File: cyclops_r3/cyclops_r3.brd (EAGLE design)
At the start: 124.5 x 79.9 mm, 113 parts, among them Q1 BC817, Q2 IRF510, U1 MCP4921, U10 ADG3301, U2 MCP4022-50k, U3 317-N, U4 TLV3701, U5 337-N, U6 ADR03, U7 OP1177, U8 LTC2052HV, U9 ZXTD45

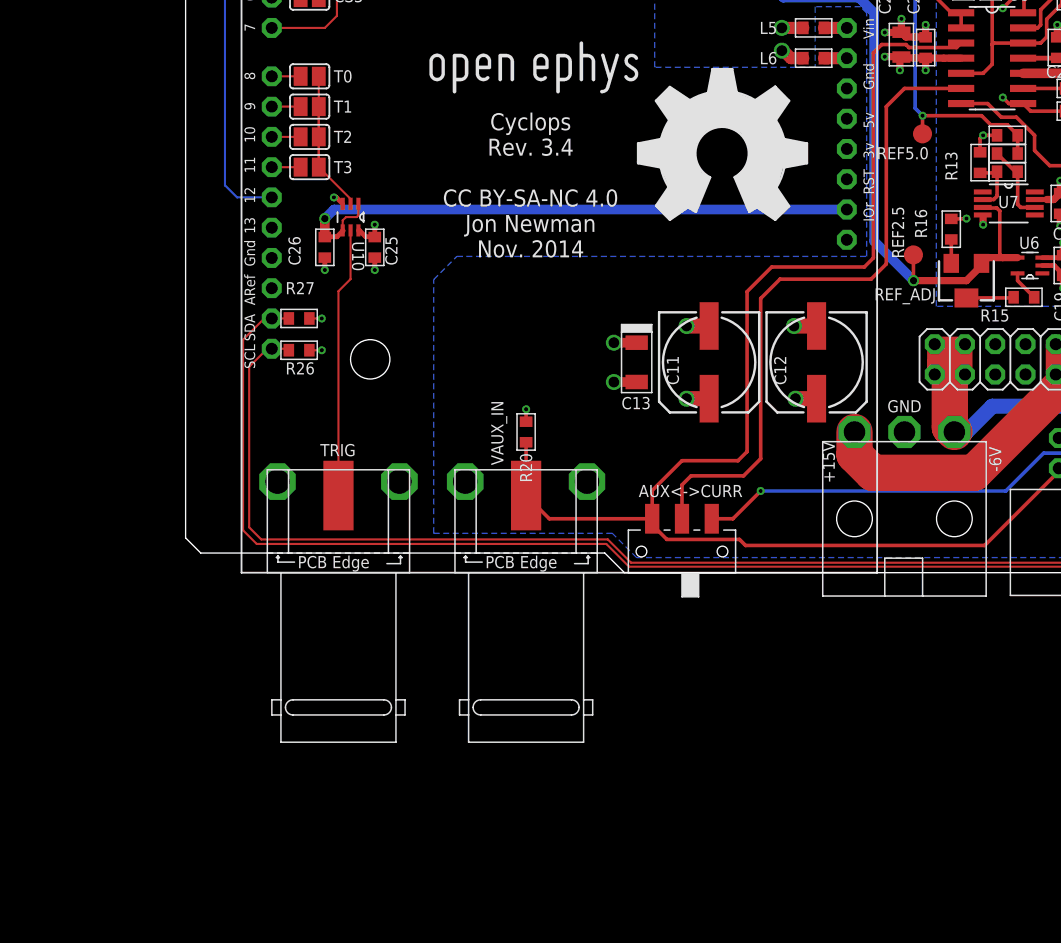
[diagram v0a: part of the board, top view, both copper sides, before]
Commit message: More spice simulations.
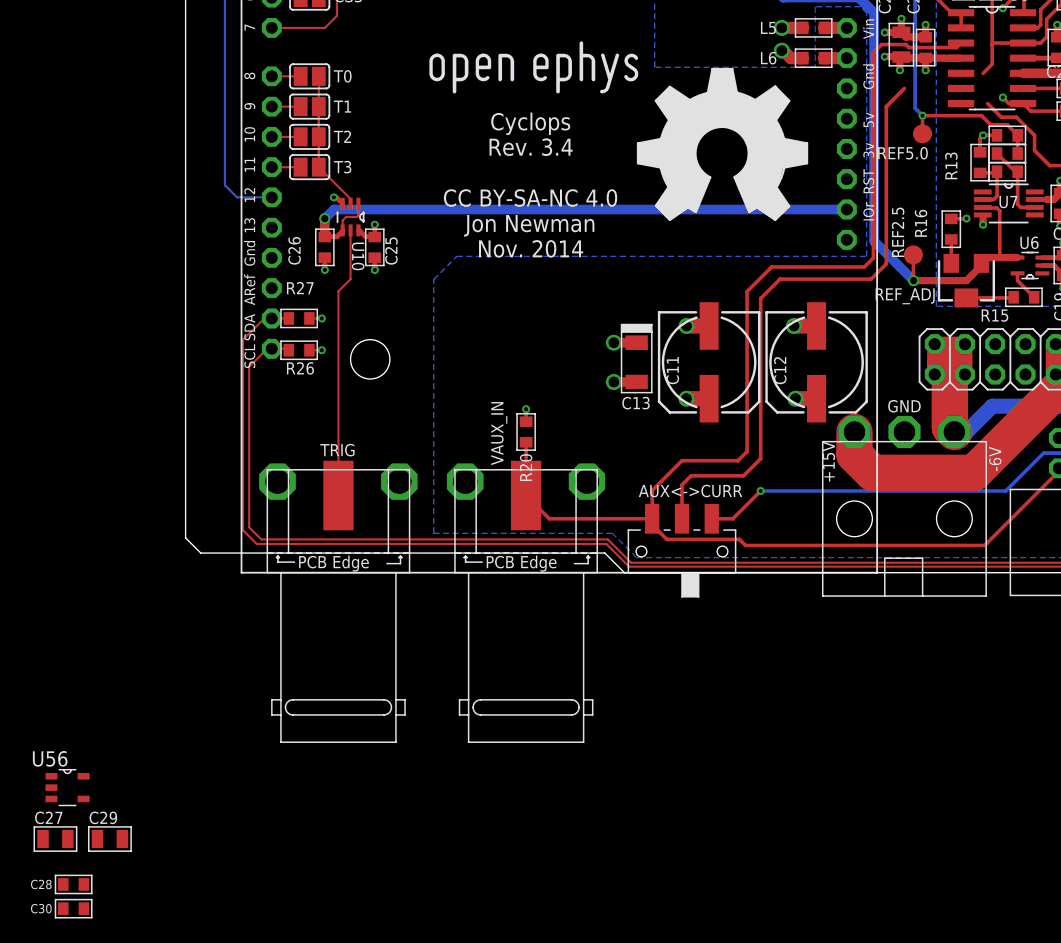
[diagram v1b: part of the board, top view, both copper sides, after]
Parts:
- added C27, C29: 1uF, cyclops:0805
- added C28, C30: .1uF, cyclops:0603
- added U56: LMP7707, cyclops:SOT95P310X175-5N
- U8: value LTC2052HV -> TLV2374
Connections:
- new net +11V1: C27.1, C28.1, D2.C, Q2.D, U9.1
- new net GND1: C27.2, C28.2, C29.2, C30.2
- new net V+: U56.5
- new net V-: U56.2
- net +11V: no longer D2.C, Q2.D, U9.1
- net -1.25V: now also C29.1, C30.1
- net N$4: now also U56.1; no longer U8.7
- net VFB: now also U56.4; no longer U8.6
- net _VREF: now also U56.3; no longer U8.5
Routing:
- net VFB: track 55.7 -> 50.9 mm
- net +11V1: track 0.00 -> 2.33 mm, vias 0 -> 2
- net +11V: track 53.7 -> 51.4 mm, vias 344 -> 342
- net N$4: track 37.5 -> 35.3 mm
- net _VREF: track 71.5 -> 69.7 mm

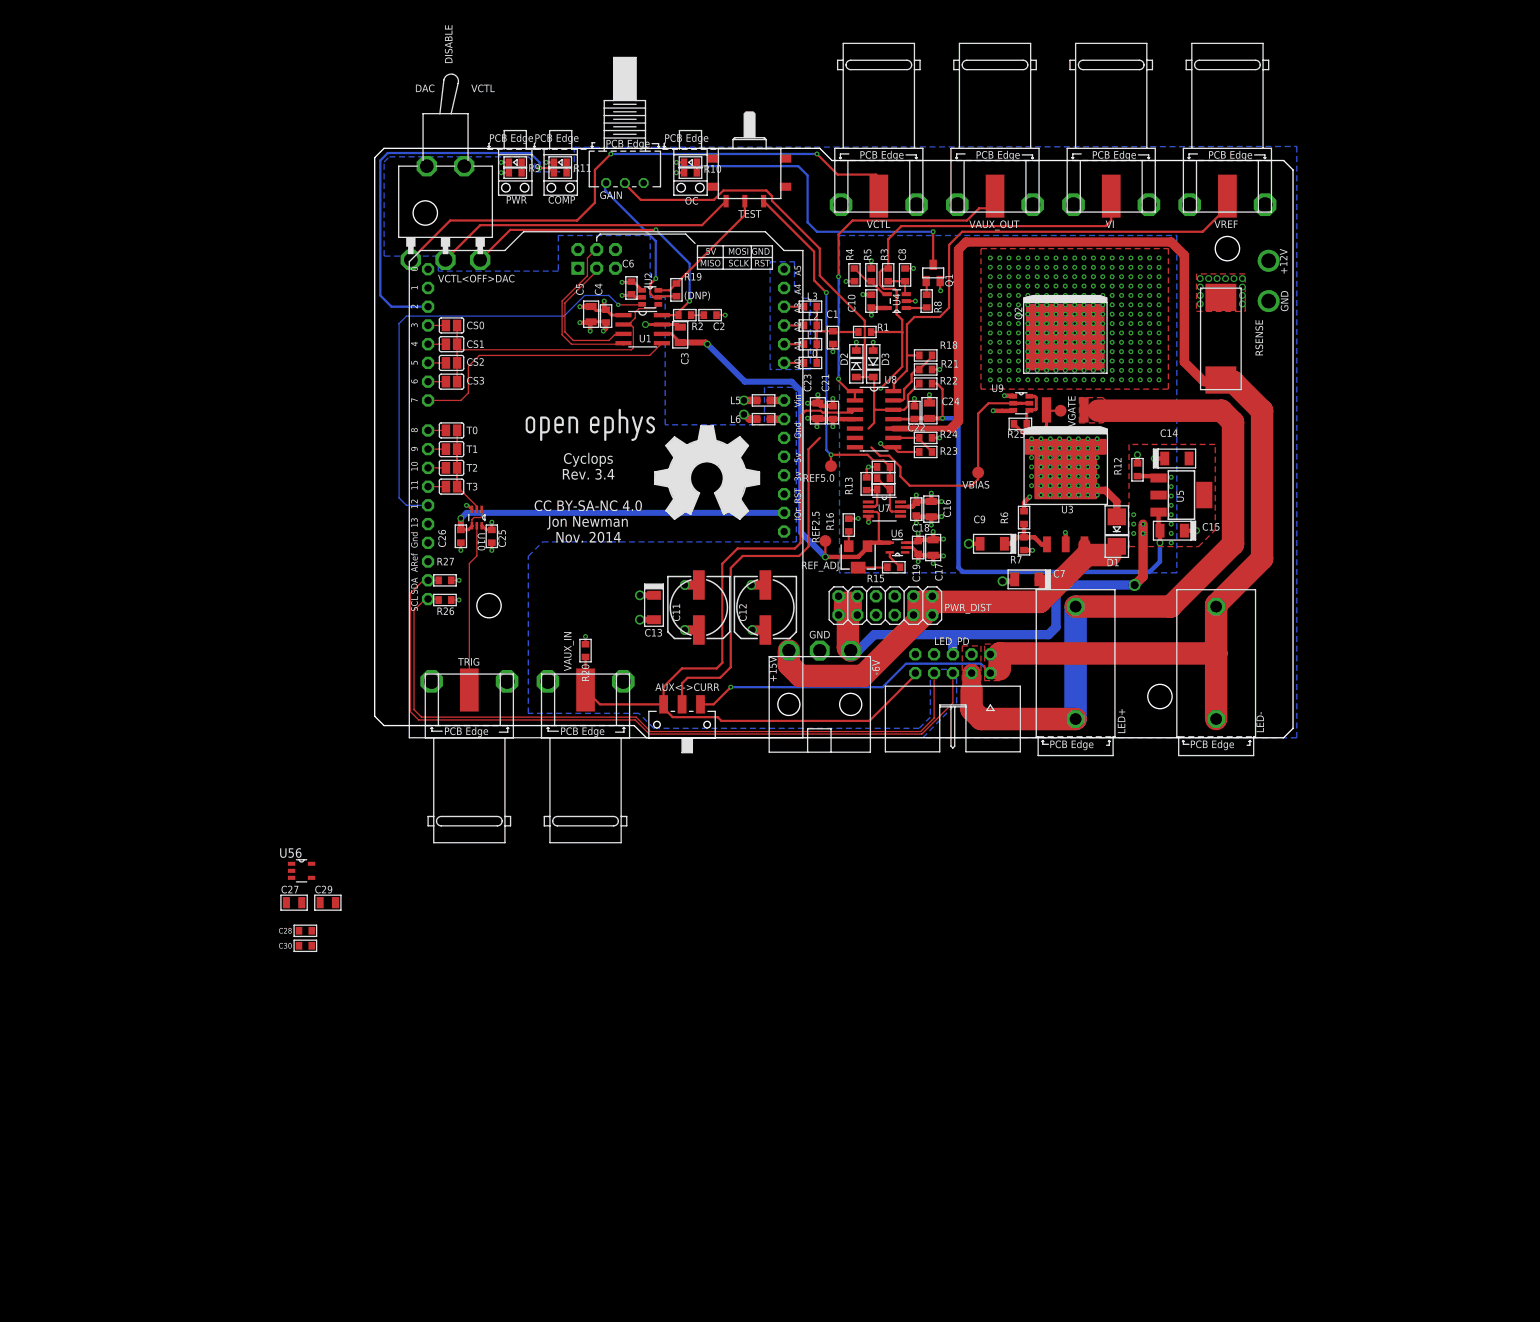
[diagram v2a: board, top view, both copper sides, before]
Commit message: Incporporated A+AB input stage into circuit.
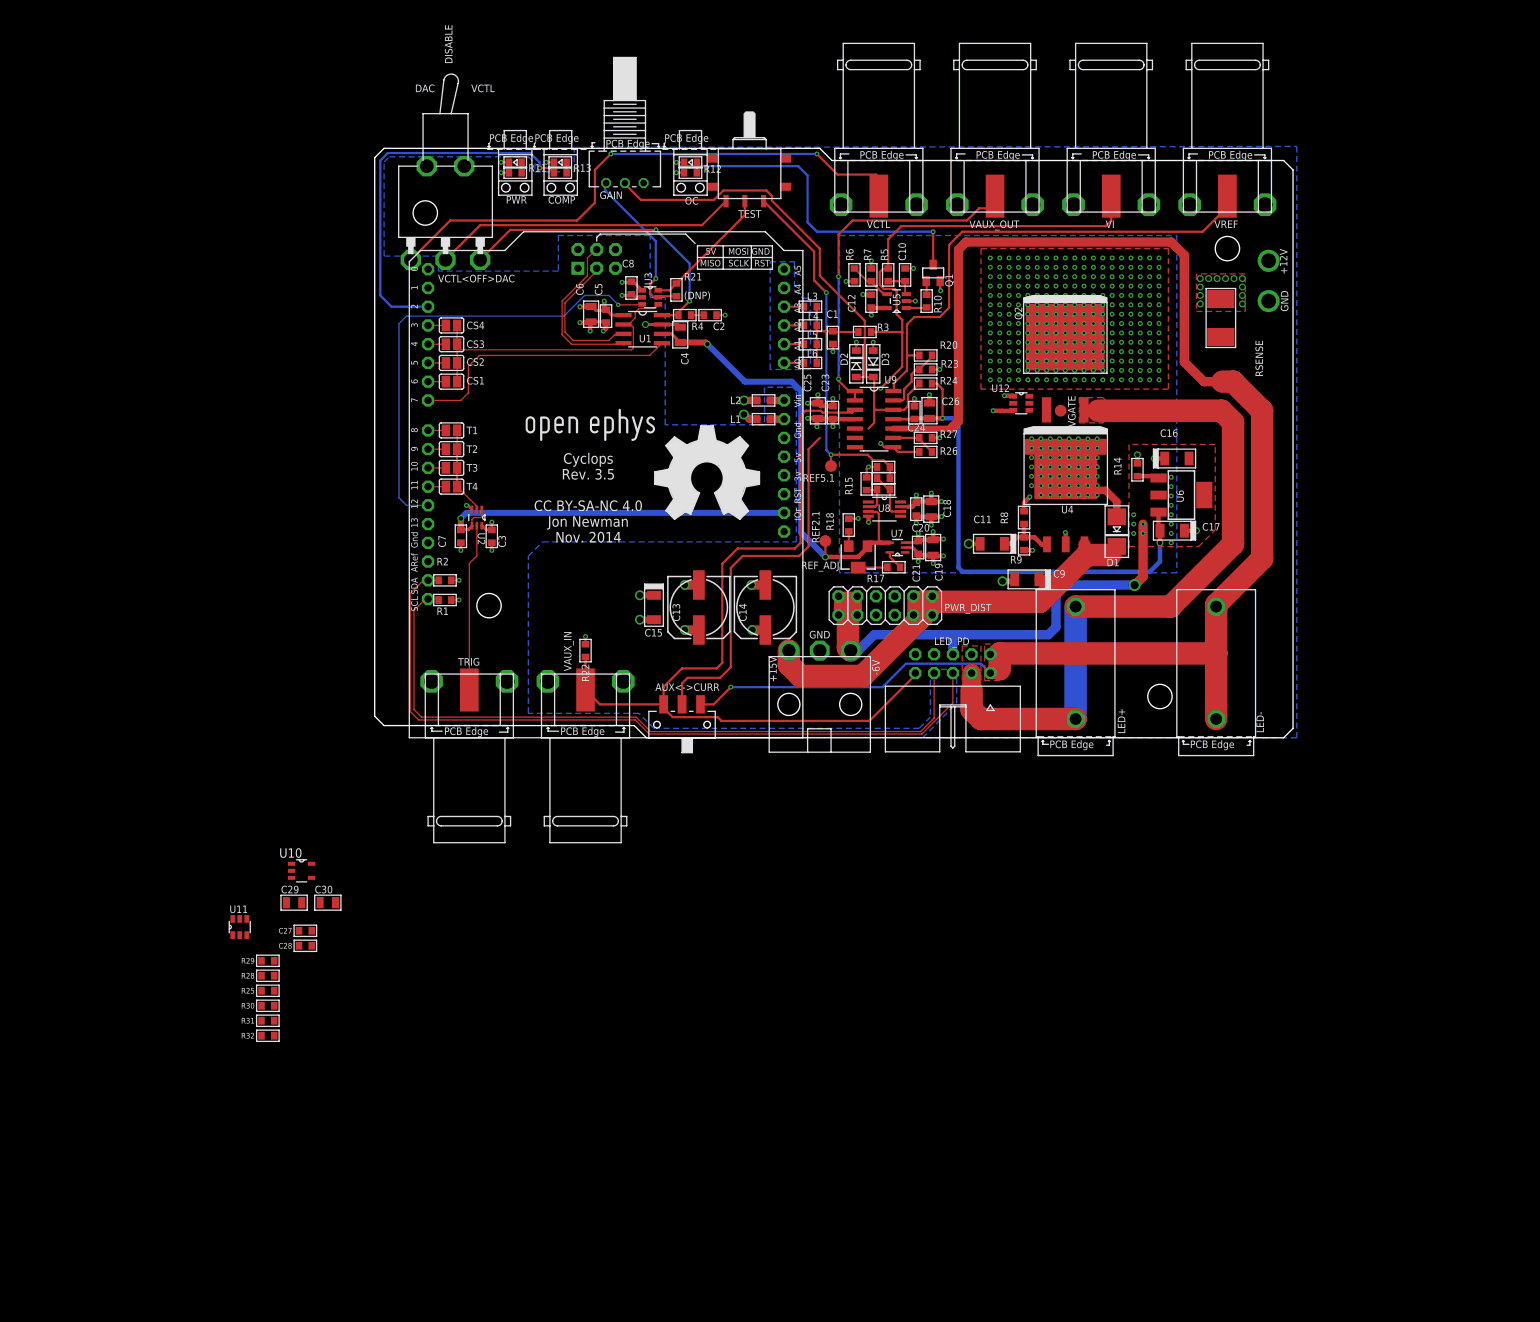
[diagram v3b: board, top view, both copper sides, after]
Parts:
- removed L0: MPZ1608, cyclops:0603
- removed T0: (no value), cyclops:SJ
- removed U56: LMP7707, cyclops:SOT95P310X175-5N
- removed VBIAS: TPTP16R, cyclops:TP16R
- added L4: MPZ1608, cyclops:0603
- added R28, R29: 2.2k, cyclops:0603
- added R30, R31: 0.5, cyclops:0603
- added R32: 10k, cyclops:0603
- added T4: (no value), cyclops:SJ
- added U11, U12: ZXTD45, cyclops:SOT23-6
- C11: value 100uF -> 10uF; device cyclops:153CLV-0807 -> cyclops:1206-POL
- C12: value 100uF -> .1uF; device cyclops:153CLV-0807 -> cyclops:0603
- C13, C14: value 1uF -> 100uF; device cyclops:1206-POL -> cyclops:153CLV-0807
- C16, C17: device cyclops:0805 -> cyclops:1206-POL
- C18, C19, C25, C26, C30, C6: value .1uF -> 1uF; device cyclops:0603 -> cyclops:0805
- C23, C24, C27, C5: value 1uF -> .1uF; device cyclops:0805 -> cyclops:0603
- C3: value 10uF -> .1uF; device cyclops:0805 -> cyclops:0603
- C4: value .1uF -> 10uF; device cyclops:0603 -> cyclops:0805
- C7: value 1uF -> .1uF; device cyclops:1206-POL -> cyclops:0603
- C9: value 10uF -> 1uF
- R1: value 100k -> 10k
- R10: value 1k -> 10k
- R11: value 1k -> 3k
- R12: value 0 -> 1k
- R14: value 1k -> 0
- R15: value 470 -> 1k
- R17: value 1k -> 470
- R19: value 5.6k -> 1k
- R2: value (none) -> 10k
- R20: value 220k -> 1k
- R21: value 1k -> 11k
- R24: value 1k -> 220k
- R25: value 10 -> 2.2k
- R26: value 10k -> 3k
- R27: value 10k -> 1k
- R3: value 10k -> 100k
- R4: value 110k -> (none)
- R6: value 240 -> 110k
- R7: value 1.82k -> 10k
- R8: value 10k -> 240
- R9: value 3k -> 1.82k
- RSENSE: value 0.5,3W -> 0.25,2W; device cyclops:PWR5322 -> cyclops:2512
- U10: value ADG3301 -> LMP7707; device cyclops:SOT65P210X110-6N -> cyclops:SOT95P310X175-5N
- U2: value MCP4022-50k -> ADG3301; device cyclops:SOT23-6 -> cyclops:SOT65P210X110-6N
- U3: value 317-N -> MCP4022-50k; device cyclops:TO-263 -> cyclops:SOT23-6
- U4: value TLV3701 -> 317-N; device ti-extended:SOT95P280X145-5N -> cyclops:TO-263
- U5: value 337-N -> TLV3701; device cyclops:SOT223 -> ti-extended:SOT95P280X145-5N
- U6: value ADR03 -> 337-N; device cyclops:SOT65P210X110-5N -> cyclops:SOT223
- U7: value OP1177 -> ADR03; device cyclops:SOP65P490X110-8N -> cyclops:SOT65P210X110-5N
- U8: value TLV2374 -> OP1177; device cyclops:SO14 -> cyclops:SOP65P490X110-8N
- U9: value ZXTD45 -> TLV2374; device cyclops:SOT23-6 -> cyclops:SO14
- moved R25 127.7 mm to (-14.5, -34.3), turned to 0 degrees
- moved R9 85.3 mm to (88.0, 26.3), turned to 90 degrees
- moved C7 76.9 mm to (11.7, 27.3), turned to 270 degrees
- moved R12 72.7 mm to (42.8, 76.6), turned to 180 degrees
- moved C15 71.0 mm to (37.9, 17.7), turned to 270 degrees
- moved R26 68.2 mm to (74.7, 38.7)
- moved R27 67.9 mm to (74.7, 40.6), turned to 0 degrees
- moved R1 67.5 mm to (9.53, 18.7)
- moved C26 65.7 mm to (75.2, 44.3), turned to 90 degrees
- moved U3 62.2 mm to (37.3, 59.7), turned to 270 degrees
- moved R20 61.0 mm to (74.7, 51.8), turned to 180 degrees
- moved C14 59.3 mm to (53.0, 17.7), turned to 270 degrees
- moved R13 59.2 mm to (25.1, 76.6), turned to 180 degrees
- moved R22 58.6 mm to (28.6, 11.8), turned to 90 degrees
- moved U10 53.4 mm to (-9.91, -18.0), turned to 0 degrees
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- renumbered CS0 to CS4, REF2.5 to REF2.1, REF5.0 to REF5.1, U$51 to X2, U$52 to X3, U$53 to X1
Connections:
- removed net +11V1: C27.1, C28.1, D2.C, Q2.D, U9.1
- removed net V+: U56.5
- removed net V-: U56.2
- new net N$24: R31.1, U12.4
- new net N$25: R30.1, U12.6
- new net N$26: Q2.G, R30.2, R31.2, R32.2
- net +11V: now also C12.1, C14.+, C15.+, C20.1, C25.1, C27.1, C29.1, D2.C, L2.2, Q2.D, R11.2, R12.2, R22.2, R28.1, R6.1, R8.2, U10.5, U11.1, U12.1, U4.2, U4.4, U5.5, U7.3, U8.7, U9.4; no longer C10.1, C11.+, C12.+, C16.1, C17.1, L5.2, R10.2, R20.2, R4.1, R6.2, R9.2, U3.2, U3.4, U4.5, U6.3, U7.7, U8.4
- net +15V: now also C9.+, U4.3; no longer C7.+, U3.3
- net +5V: now also C3.1, C8.1, R1.1, R2.1, U2.6, U3.1; no longer C25.1, C4.1, R26.1, R27.1, U10.6, U2.1
- net -1.25V: now also C17.-, C26.1, C28.1, R24.1, R25.2, R29.2, U10.2, U11.3, U12.3, U6.3, U9.11; no longer C15.-, C22.1, C29.1, R22.1, U5.3, U8.11
- net -6V: now also C16.-, U6.4; no longer C14.-, U5.4
- net COMP+: now also C10.1, R5.1, U5.3; no longer C8.1, R3.1, U4.3
- net CS: now also U3.4; no longer U2.4
- net CS1: now also CS3.1; no longer CS1.1
- net CS3: now also CS1.1; no longer CS3.1
- net DACA: now also R4.2; no longer R2.2
- net GND: now also C12.2, C14.-, C15.-, C16.+, C17.+, C7.2, L1.2, R14.2, R15.2, R18.1, R23.2, R27.2, R32.1, R7.2, R9.1, U2.3, U3.2, U5.2, U7.2, U8.4; no longer C12.-, C14.+, C15.+, C16.2, C17.2, C7.-, L6.2, R12.2, R13.2, R16.1, R21.2, R24.2, R5.2, R7.1, U10.3, U2.2, U4.2, U6.2, U7.4, U9.3
- net KEEPOUT_GND: now also L1.1; no longer L6.1
- net LED-: now also U9.10; no longer U8.10
- net N$1: now also R4.1; no longer R2.1
- net N$10: now also R29.1, U11.6, U12.5; no longer R25.1, U9.4, U9.6
- net N$11: now also L4.2, L5.2, L6.2, R3.2; no longer L0.2, L1.2, L2.2, R1.2
- net N$12: now also R14.1, U6.1; no longer R12.1, U5.1
- net N$13: now also R25.1, U10.1, U11.2, U11.5; no longer Q2.G, R25.2, VGATE.TP
- net N$14: now also L2.1; no longer L5.1
- net N$15: now also R26.1, R27.1, U9.9; no longer R23.1, R24.1, U8.9
- net N$16: now also R13.1; no longer R11.1
- net N$18: now also R15.1, R16.2, U8.2; no longer R13.1, R14.2, U7.2
- net N$19: now also L5.1; no longer L1.1
- net N$2: now also R12.1; no longer R10.1
- net N$20: now also R17.2, U7.5; no longer R15.2, U6.5
- net N$21: now also L4.1; no longer L2.1
- net N$22: now also R17.1; no longer R15.1
- net N$27: now also R10.2, U5.1; no longer R8.2, U4.1
- net N$28: now also R10.1; no longer R8.1
- net N$3: now also R11.1; no longer R9.1
- net N$4: now also R28.2, U11.4, U12.2; no longer U56.1, U9.2, U9.5, VBIAS.TP
- net N$5: now also R6.2, R7.1, U5.4; no longer R4.2, R5.1, U4.4
- net N$6: now also R18.2; no longer R16.2
- net N$7: now also L6.1; no longer L0.1
- net N$72: now also C11.+, R8.1, R9.2, U4.1; no longer C9.+, R6.1, R7.2, U3.1
- net N$8: now also R20.1, R23.1, U9.13; no longer R18.1, R21.1, U8.13
- net OC_COMP: now also R13.2; no longer R11.2
- net POT: now also U3.3; no longer U2.3
- net REF2.5: now also C4.1, U7.4, U8.3; no longer C3.1, U6.4, U7.3
- net REF5.0: now also C22.1, R19.2; no longer C20.1, R17.2
- net SCL: now also R1.2; no longer R26.2
- net SDA: now also R2.2; no longer R27.2
- net T0: now also T1.2; no longer T0.2
- net T1: now also T2.2; no longer T1.2
- net T2: now also T3.2; no longer T2.2
- net T3: now also T4.2; no longer T3.2
- net TRIG: now also T4.1, U2.2; no longer T0.1, U10.2
- net TRIG_EXT: now also U2.5; no longer U10.5
- net VAUX: now also R22.1, U9.3; no longer R20.1, U8.3
- net VAUX_OUT: now also U9.1, U9.2; no longer U8.1, U8.2
- net VCTL: now also R21.2, U3.6; no longer R19.2, U2.6
- net VCTL_PROTECT: now also R21.1, U3.5; no longer R19.1, U2.5
- net VFB: now also U10.4; no longer U56.4
- net VI: now also R26.2, R3.1, R5.2, U9.8; no longer R1.1, R23.2, R3.2, U8.8
- net VLOGIC: now also C7.1, U2.1, U2.4; no longer C26.1, U10.1, U10.4
- net VREF: now also R20.2, U9.14; no longer R18.2, U8.14
- net VREFA2X1: now also R16.1, R19.1, U8.6; no longer R14.1, R17.1, U7.6
- net _VREF: now also R24.2, U10.3, U9.12; no longer R22.2, U56.3, U8.12
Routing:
- net N$4: track 35.3 -> 0.00 mm
- net N$13: track 9.58 -> 0.00 mm
- net N$10: track 5.53 -> 0.00 mm
- net -1.25V: track 70.4 -> 73.2 mm, vias 2 -> 3
- net GND: track 114.2 -> 111.4 mm, vias 58 -> 57
- net +11V1: track 2.33 -> 0.00 mm, vias 2 -> 0
- net +11V: track 51.4 -> 53.7 mm, vias 342 -> 344
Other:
- board text added: "Cyclops Rev. 3.5 CC BY-SA-NC 4.0 Jon Newman Nov. 2014"
- board text removed: "Cyclops Rev. 3.4 CC BY-SA-NC 4.0 Jon Newman Nov. 2014"
